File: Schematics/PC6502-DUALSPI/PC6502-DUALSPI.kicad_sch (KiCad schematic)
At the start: 20 parts, among them J1 BUS, J5 Conn_02x05_Odd_Even, U1 ATF1502AS, X2 CXO_DIP8

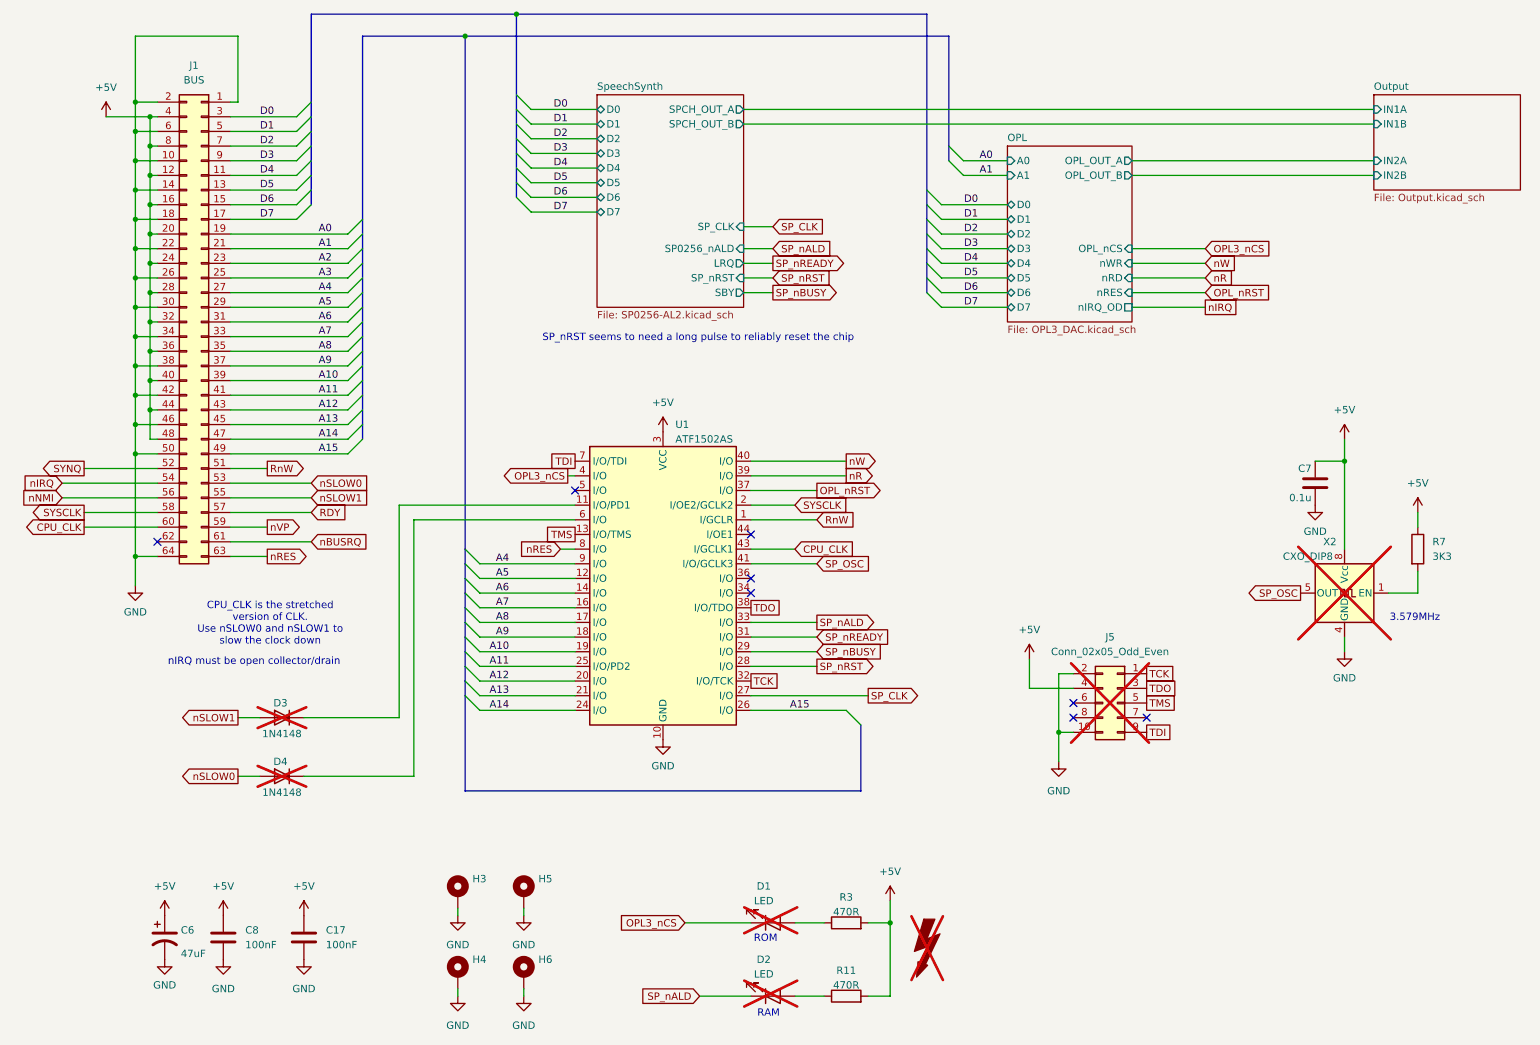
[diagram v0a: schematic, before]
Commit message: Ordered Storage, FM/Speech, Dual SPI and APPLE II slot PCBs
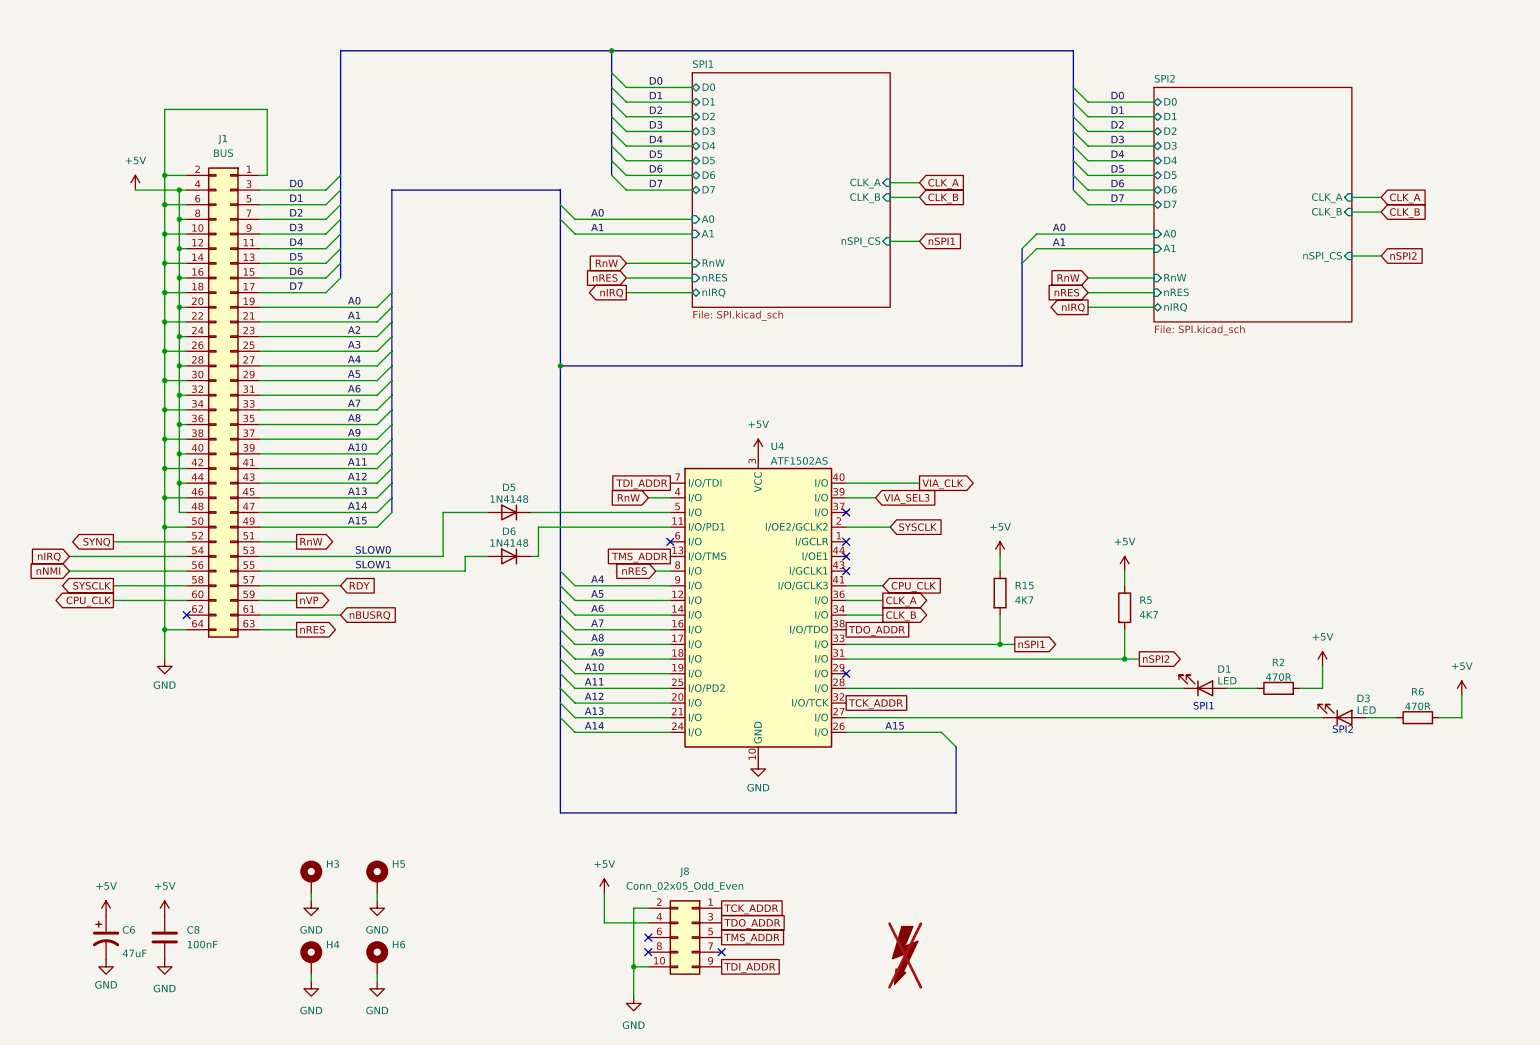
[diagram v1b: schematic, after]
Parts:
- removed C17: 100nF, Capacitor_SMD:C_0603_1608Metric, symbol Device:C
- removed C7: 0.1u, Capacitor_SMD:C_0603_1608Metric, symbol Device:C
- removed D2: LED, LTL-4221NHBP:LTL4221NHBP, symbol Device:LED
- removed D3, D4: 1N4148, Diode_THT:D_DO-35_SOD27_P7.62mm_Horizontal, symbol Diode:1N4148
- removed J5: Conn_02x05_Odd_Even, Connector_PinHeader_2.54mm:PinHeader_2x05_P2.54mm_Vertical, symbol Connector_Generic:Conn_02x05_Odd_Even
- removed R11, R3: 470R, Resistor_SMD:R_0603_1608Metric_Pad0.98x0.95mm_HandSolder, symbol Device:R
- removed R7: 3K3, Resistor_SMD:R_0603_1608Metric_Pad0.98x0.95mm_HandSolder, symbol Device:R
- removed U1: ATF1502AS, Package_LCC:PLCC-44_THT-Socket, symbol PaulasKiCAD:ATF1502AS_PLCC
- removed X2: CXO_DIP8, Oscillator:Oscillator_DIP-8, symbol Oscillator:CXO_DIP8
- added D3: LED, LTL-4221NHBP:LTL4221NHBP, symbol Device:LED
- added D5, D6: 1N4148, Diode_THT:D_DO-35_SOD27_P7.62mm_Horizontal, symbol Diode:1N4148
- added J8: Conn_02x05_Odd_Even, Connector_PinHeader_2.54mm:PinHeader_2x05_P2.54mm_Vertical, symbol Connector_Generic:Conn_02x05_Odd_Even
- added R15, R5: 4K7, Resistor_SMD:R_0603_1608Metric_Pad0.98x0.95mm_HandSolder, symbol Device:R
- added R2, R6: 470R, Resistor_SMD:R_0603_1608Metric_Pad0.98x0.95mm_HandSolder, symbol Device:R
- added U4: ATF1502AS, Package_LCC:PLCC-44_THT-Socket, symbol PaulasKiCAD:ATF1502AS_PLCC
- C8: footprint Capacitor_SMD:C_0603_1608Metric -> Capacitor_SMD:C_0805_2012Metric
- D1: LCSC DNF -> (none); now fitted
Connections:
- net +5V: now also J8.4 (Pin_4), R15.1, R2.2, R5.1, R6.2, U4.15 (VCC), U4.23 (VCC), U4.3 (VCC), U4.35 (VCC)
- net A10: now also U4.19 (I/O)
- net A11: now also U4.25 (I/O/PD2)
- net A12: now also U4.20 (I/O)
- net A13: now also U4.21 (I/O)
- net A14: now also U4.24 (I/O)
- net A15: now also U4.26 (I/O)
- net A4: now also U4.9 (I/O)
- net A5: now also U4.12 (I/O)
- net A6: now also U4.14 (I/O)
- net A7: now also U4.16 (I/O)
- net A8: now also U4.17 (I/O)
- net A9: now also U4.18 (I/O)
- net CPU_CLK: now also U4.41 (I/O/GCLK3)
- net GND: now also J8.10 (Pin_10), J8.2 (Pin_2), U4.10 (GND), U4.22 (GND), U4.30 (GND), U4.42 (GND)
- net RnW: now also U4.4 (I/O)
- net SYSCLK: now also U4.2 (I/OE2/GCLK2)
- net nRES: now also U4.8 (I/O)
- net at D1.2 (A): now also R2.1
- net OPL3_nCS: no longer names the net of D1.1 (K)
- net OPL3_nCS: now also U4.28 (I/O)
- net nSLOW0 renamed SLOW0
- net SLOW0: now also D5.2 (A)
- net nSLOW1 renamed SLOW1
- net SLOW1: now also D6.2 (A)
- new net: D6.1 (K), U4.11 (I/O/PD1)
- new net: D5.1 (K), U4.5 (I/O)
- new net: D3.1 (K), U4.27 (I/O)
- new net: D3.2 (A), R6.1
- new net CLK_A: U4.36 (I/O)
- new net CLK_B: U4.34 (I/O)
- new net TCK_ADDR: J8.1 (Pin_1), U4.32 (I/O/TCK)
- new net TDI_ADDR: J8.9 (Pin_9), U4.7 (I/O/TDI)
- new net TDO_ADDR: J8.3 (Pin_3), U4.38 (I/O/TDO)
- new net TMS_ADDR: J8.5 (Pin_5), U4.13 (I/O/TMS)
- new net VIA_CLK: U4.40 (I/O)
- new net VIA_SEL3: U4.39 (I/O)
- new net nSPI1: R15.2, U4.33 (I/O)
- new net nSPI2: R5.2, U4.31 (I/O)
- no-connect marks 8 -> 10
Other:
- removed sheet OPL
- removed sheet Output
- removed sheet SpeechSynth
- added sheet SPI1 (SPI.kicad_sch)
- added sheet SPI2 (SPI.kicad_sch)
- note added: "SPI1"
- note added: "SPI2"
- note removed: "3.579MHz"
- note removed: "CPU_CLK is the stretched version of CLK. Use nSLOW0 and nSLOW1 to slow the clock down"
- note removed: "RAM"
- note removed: "ROM"
- note removed: "SP_nRST seems to need a long pulse to reliably reset the chip"
- note removed: "nIRQ must be open collector/drain"
- moved on the sheet: C6, C8, H3, H4, H5, H6, J1
